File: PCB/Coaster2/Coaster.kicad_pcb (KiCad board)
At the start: 2 copper layers, 120 x 120 mm, 277 parts, among them J1 Reset, J2 TC2030-USB-NL-DS, J3 USB-C-Socket-H, U1 ICS43434_MEMS_Mic, U2 ESP32-S3-MINI-1, U3 MD8942

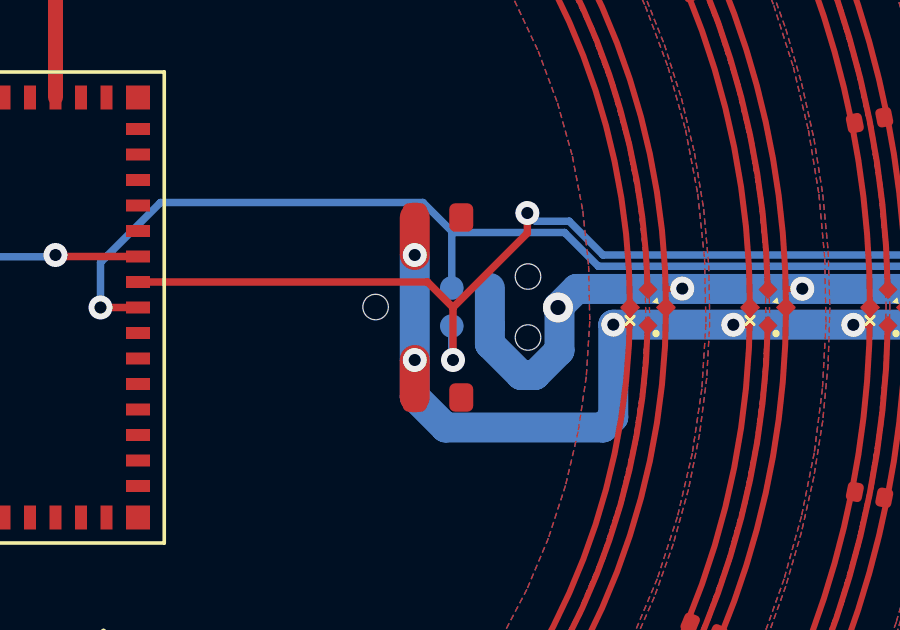
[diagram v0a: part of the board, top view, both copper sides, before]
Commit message: Fixed render
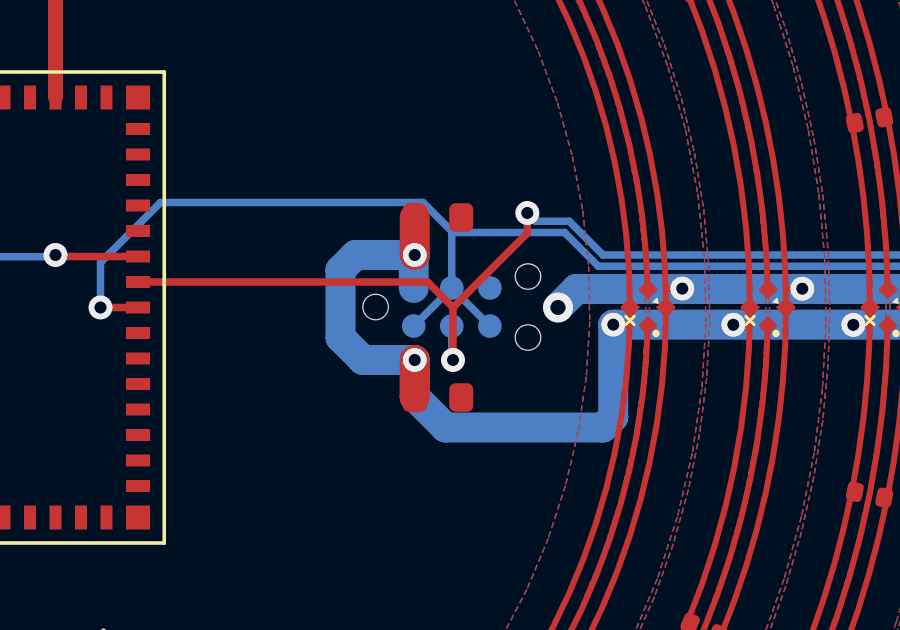
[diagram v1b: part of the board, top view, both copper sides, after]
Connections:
- J2 pad 2: VBUS -> D-
- J2 pad 6: GND -> D-
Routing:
- net GND: track 1099.9 -> 1093.5 mm
- net VBUS: track 1079.2 -> 1084.6 mm
- net D-: track 48.7 -> 52.3 mm
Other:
- board text added: "TC2030"

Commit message: Tidy
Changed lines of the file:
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@@
 	)
 	(gr_circle
+		(center 100 100)
+		(end 148 99.6)
+		(stroke
+			(width 1)
+			(type dot)
+		)
+		(fill no)
+		(layer "F.Mask")
+	)
+	(gr_circle
 		(center 80 134.641)
 		(end 85 134.641)
@@
 	)
 	(gr_circle
+		(center 100 100)
+		(end 78 100)
+		(stroke
+			(width 0.12)
+			(type dot)
+		)
+		(fill no)
+		(layer "B.SilkS")
+	)
+	(gr_circle
 		(center 140 100)
 		(end 140 95)
@@
 	)
 	(gr_circle
+		(center 100 100)
+		(end 51 100)
+		(stroke
+			(width 0.12)
+			(type dot)
+		)
+		(fill no)
+		(layer "B.SilkS")
+	)
+	(gr_circle
 		(center 140 100)
 		(end 143 100)
@@
 	)
 	(zone
-		(net 113)
-		(net_name "SD")
-		(layer "F.Cu")
-		(name "$teardrop_padvia$")
-		(hatch full 0.1)
-		(priority 30002)
-		(attr
-			(teardrop
-				(type padvia)
-			)
-		)
-		(connect_pads yes
-			(clearance 0)
-		)
-		(min_thickness 0.0254)
-		(filled_areas_thickness no)
-		(fill yes
-			(thermal_gap 0.5)
-			(thermal_bridge_width 0.5)
-			(island_removal_mode 1)
-			(island_area_min 10)
-		)
-		(polygon
-			(pts
-				(xy 100.334564 84.300341) (xy 100.511341 84.123564) (xy 100.3 83.71989) (xy 99.999293 83.788293)
-				(xy 99.89189 84.05)
-			)
-		)
-	)
-	(zone
 		(net 1)
 		(net_name "GND")
@@
 	)
 	(zone
-		(net 114)
-		(net_name "WS")
-		(layer "F.Cu")
-		(name "$teardrop_padvia$")
-		(hatch full 0.1)
-		(priority 30003)
-		(attr
-			(teardrop
-				(type padvia)
-			)
-		)
-		(connect_pads yes
-			(clearance 0)
-		)
-		(min_thickness 0.0254)
-		(filled_areas_thickness no)
-		(fill yes
-			(thermal_gap 0.5)
-			(thermal_bridge_width 0.5)
-			(island_removal_mode 1)
-			(island_area_min 10)
-		)
-		(polygon
-			(pts
-				(xy 100.775 84.311) (xy 101.025 84.311) (xy 101.161 84.012296) (xy 100.9 83.788) (xy 100.639 84.012296)
-			)
-		)
-	)
-	(zone
-		(net 2)
-		(net_name "+3V3")
-		(layer "F.Cu")
-		(name "$teardrop_padvia$")
-		(hatch full 0.1)
-		(priority 30000)
-		(attr
-			(teardrop
-				(type padvia)
-			)
-		)
-		(connect_pads yes
-			(clearance 0)
-		)
-		(min_thickness 0.0254)
-		(filled_areas_thickness no)
-		(fill yes
-			(thermal_gap 0.5)
-			(thermal_bridge_width 0.5)
-			(island_removal_mode 1)
-			(island_area_min 10)
-		)
-		(polygon
-			(pts
-				(xy 103.1625 111.6) (xy 103.103596 111.600725) (xy 102.907165 111.599072) (xy 102.798558 111.588917)
-				(xy 102.69297 111.567298) (xy 102.59786 111.53028) (xy 102.520689 111.473931) (xy 102.468915 111.394315)
-				(xy 102.454884 111.344553) (xy 102.45 111.2875) (xy 100.599 112) (xy 102.45 112.7125) (xy 102.454846 112.655657)
-				(xy 102.468771 112.60605) (xy 102.51997 112.526809) (xy 102.603622 112.466746) (xy 102.72734 112.423986)
-				(xy 102.9006 112.401291) (xy 103.103596 112.399275) (xy 103.1625 112.4)
-			)
-		)
-	)
-	(zone
 		(net 1)
 		(net_name "GND")
@@
 	)
 	(zone
+		(net 113)
+		(net_name "SD")
+		(layer "F.Cu")
+		(name "$teardrop_padvia$")
+		(hatch full 0.1)
+		(priority 30002)
+		(attr
+			(teardrop
+				(type padvia)
+			)
+		)
+		(connect_pads yes
+			(clearance 0)
+		)
+		(min_thickness 0.0254)
+		(filled_areas_thickness no)
+		(fill yes
+			(thermal_gap 0.5)
+			(thermal_bridge_width 0.5)
+			(island_removal_mode 1)
+			(island_area_min 10)
+		)
+		(polygon
+			(pts
+				(xy 100.334564 84.300341) (xy 100.511341 84.123564) (xy 100.3 83.71989) (xy 99.999293 83.788293)
+				(xy 99.89189 84.05)
+			)
+		)
+	)
+	(zone
+		(net 114)
+		(net_name "WS")
+		(layer "F.Cu")
+		(name "$teardrop_padvia$")
+		(hatch full 0.1)
+		(priority 30003)
+		(attr
+			(teardrop
+				(type padvia)
+			)
+		)
+		(connect_pads yes
+			(clearance 0)
+		)
+		(min_thickness 0.0254)
+		(filled_areas_thickness no)
+		(fill yes
+			(thermal_gap 0.5)
+			(thermal_bridge_width 0.5)
+			(island_removal_mode 1)
+			(island_area_min 10)
+		)
+		(polygon
+			(pts
+				(xy 100.775 84.311) (xy 101.025 84.311) (xy 101.161 84.012296) (xy 100.9 83.788) (xy 100.639 84.012296)
+			)
+		)
+	)
+	(zone
+		(net 2)
+		(net_name "+3V3")
+		(layer "F.Cu")
+		(name "$teardrop_padvia$")
+		(hatch full 0.1)
+		(priority 30000)
+		(attr
+			(teardrop
+				(type padvia)
+			)
+		)
+		(connect_pads yes
+			(clearance 0)
+		)
+		(min_thickness 0.0254)
+		(filled_areas_thickness no)
+		(fill yes
+			(thermal_gap 0.5)
+			(thermal_bridge_width 0.5)
+			(island_removal_mode 1)
+			(island_area_min 10)
+		)
+		(polygon
+			(pts
+				(xy 103.1625 111.6) (xy 103.103596 111.600725) (xy 102.907165 111.599072) (xy 102.798558 111.588917)
+				(xy 102.69297 111.567298) (xy 102.59786 111.53028) (xy 102.520689 111.473931) (xy 102.468915 111.394315)
+				(xy 102.454884 111.344553) (xy 102.45 111.2875) (xy 100.599 112) (xy 102.45 112.7125) (xy 102.454846 112.655657)
+				(xy 102.468771 112.60605) (xy 102.51997 112.526809) (xy 102.603622 112.466746) (xy 102.72734 112.423986)
+				(xy 102.9006 112.401291) (xy 103.103596 112.399275) (xy 103.1625 112.4)
+			)
+		)
+	)
+	(zone
+		(net 1)
+		(net_name "GND")
+		(layers "F&B.Cu")
+		(hatch edge 0.5)
+		(priority 1)
+		(connect_pads
+			(clearance 0.127)
+		)
+		(min_thickness 0.25)
+		(filled_areas_thickness no)
+		(fill yes
+			(thermal_gap 0.5)
+			(thermal_bridge_width 0.5)
+		)
+		(polygon
+			(pts
+				(xy 50 50) (xy 150 50) (xy 150 150) (xy 50 150)
+			)
+		)
+	)
+	(zone
 		(net 0)
 		(net_name "")
@@
 		(name "$teardrop_padvia$")
 		(hatch full 0.1)
-		(priority 30001)
-		(attr
-			(teardrop
-				(type padvia)
-			)
-		)
-		(connect_pads yes
-			(clearance 0)
-		)
-		(min_thickness 0.0254)
-		(filled_areas_thickness no)
-		(fill yes
-			(thermal_gap 0.5)
-			(thermal_bridge_width 0.5)
-			(island_removal_mode 1)
-			(island_area_min 10)
-		)
-		(polygon
-			(pts
-				(xy 118.266962 99.979185) (xy 118.090185 100.155962) (xy 118.40265 100.837728) (xy 118.730707 100.619707)
-				(xy 118.948728 100.29165)
-			)
-		)
-	)
-	(zone
-		(net 110)
-		(net_name "D-")
-		(layer "B.Cu")
-		(name "$teardrop_padvia$")
-		(hatch full 0.1)
 		(priority 30003)
 		(attr
@@
 		(name "$teardrop_padvia$")
 		(hatch full 0.1)
-		(priority 30005)
+		(priority 30001)
 		(attr
 			(teardrop
@@
 		(polygon
 			(pts
-				(xy 117.585 98.569165) (xy 117.335 98.569165) (xy 117.073865 99.272193) (xy 117.46 99.35) (xy 117.846135 99.272193)
+				(xy 118.266962 99.979185) (xy 118.090185 100.155962) (xy 118.40265 100.837728) (xy 118.730707 100.619707)
+				(xy 118.948728 100.29165)
+			)
+		)
+	)
+	(zone
+		(net 106)
+		(net_name "D+")
+		(layer "B.Cu")
+		(name "$teardrop_padvia$")
+		(hatch full 0.1)
+		(priority 30004)
+		(attr
+			(teardrop
+				(type padvia)
+			)
+		)
+		(connect_pads yes
+			(clearance 0)
+		)
+		(min_thickness 0.0254)
+		(filled_areas_thickness no)
+		(fill yes
+			(thermal_gap 0.5)
+			(thermal_bridge_width 0.5)
+			(island_removal_mode 1)
+			(island_area_min 10)
+		)
+		(polygon
+			(pts
+				(xy 117.335 101.398835) (xy 117.585 101.398835) (xy 117.846135 100.695807) (xy 117.46 100.618) (xy 117.073865 100.695807)
 			)
 		)
@@
 	)
 	(zone
-		(net 1)
-		(net_name "GND")
+		(net 110)
+		(net_name "D-")
 		(layer "B.Cu")
-		(hatch edge 0.5)
-		(priority 1)
-		(connect_pads
-			(clearance 0.127)
+		(name "$teardrop_padvia$")
+		(hatch full 0.1)
+		(priority 30005)
+		(attr
+			(teardrop
+				(type padvia)
+			)
 		)
-		(min_thickness 0.25)
+		(connect_pads yes
+			(clearance 0)
+		)
+		(min_thickness 0.0254)
 		(filled_areas_thickness no)
 		(fill yes
 			(thermal_gap 0.5)
 			(thermal_bridge_width 0.5)
+			(island_removal_mode 1)
+			(island_area_min 10)
 		)
 		(polygon
 			(pts
-				(xy 50 50) (xy 150 50) (xy 150 150) (xy 50 150)
+				(xy 117.585 98.569165) (xy 117.335 98.569165) (xy 117.073865 99.272193) (xy 117.46 99.35) (xy 117.846135 99.272193)
 			)
 		)
@@
 		(name "$teardrop_padvia$")
 		(hatch full 0.1)
-		(priority 30002)
+		(priority 30000)
 		(attr
 			(teardrop
@@
 		(polygon
 			(pts
-				(xy 116.829815 100.155962) (xy 116.653038 99.979185) (xy 115.971272 100.29165) (xy 116.189293 100.619707)
-				(xy 116.51735 100.837728)
+				(xy 117.923038 99.988815) (xy 118.099815 99.812038) (xy 117.78735 99.130272) (xy 117.459293 99.348293)
+				(xy 117.241272 99.67635)
 			)
 		)
 	)
 	(zone
-		(net 106)
-		(net_name "D+")
+		(net 110)
+		(net_name "D-")
 		(layer "B.Cu")
 		(name "$teardrop_padvia$")
 		(hatch full 0.1)
-		(priority 30004)
+		(priority 30002)
 		(attr
 			(teardrop
@@
 		(polygon
 			(pts
-				(xy 117.335 101.398835) (xy 117.585 101.398835) (xy 117.846135 100.695807) (xy 117.46 100.618) (xy 117.073865 100.695807)
+				(xy 116.829815 100.155962) (xy 116.653038 99.979185) (xy 115.971272 100.29165) (xy 116.189293 100.619707)
+				(xy 116.51735 100.837728)
 			)
 		)
@@
 			)
 		)
-	)
-	(zone
-		(net 110)
-		(net_name "D-")
-		(layer "B.Cu")
-		(name "$teardrop_padvia$")
-		(hatch full 0.1)
-		(priority 30000)
-		(attr
-			(teardrop
-				(type padvia)
-			)
-		)
-		(connect_pads yes
-			(clearance 0)
-		)
-		(min_thickness 0.0254)
-		(filled_areas_thickness no)
-		(fill yes
-			(thermal_gap 0.5)
-			(thermal_bridge_width 0.5)
-			(island_removal_mode 1)
-			(island_area_min 10)
-		)
-		(polygon
-			(pts
-				(xy 117.923038 99.988815) (xy 118.099815 99.812038) (xy 117.78735 99.130272) (xy 117.459293 99.348293)
-				(xy 117.241272 99.67635)
-			)
-		)

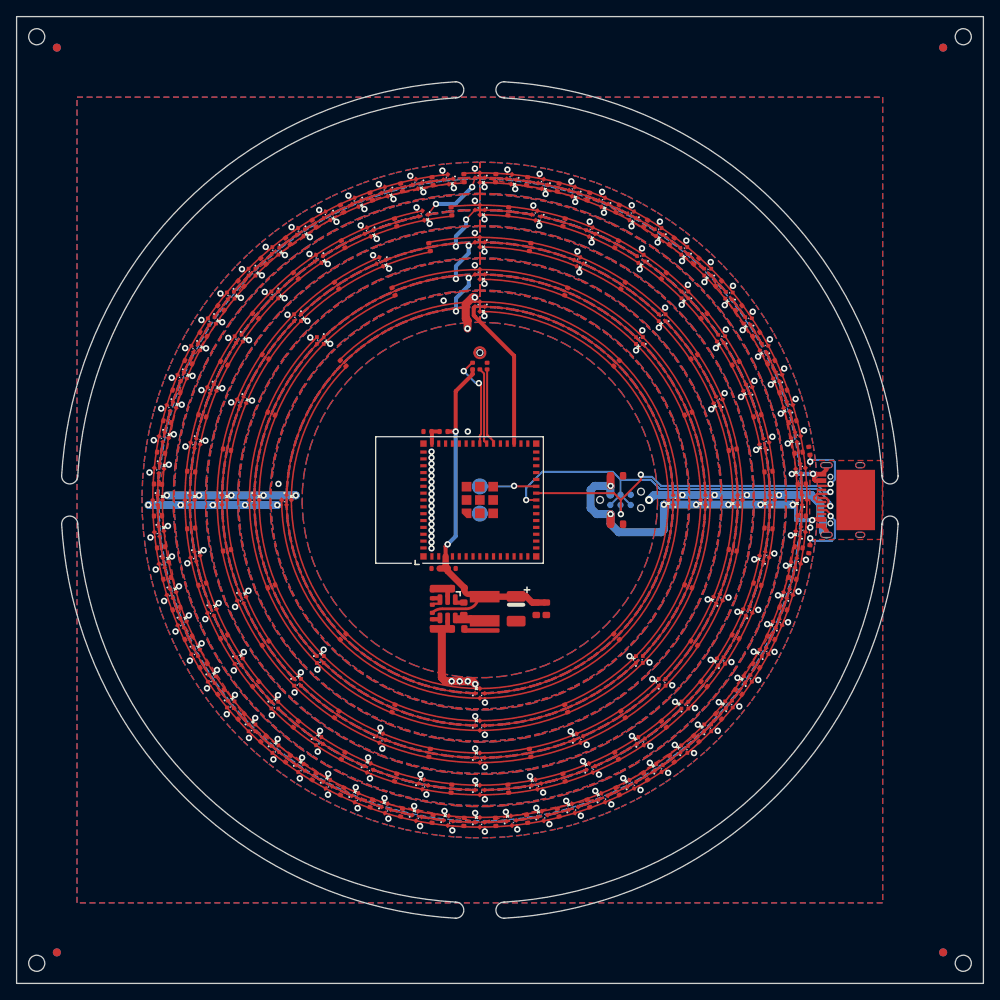
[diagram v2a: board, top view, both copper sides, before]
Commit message: WAGO power pads
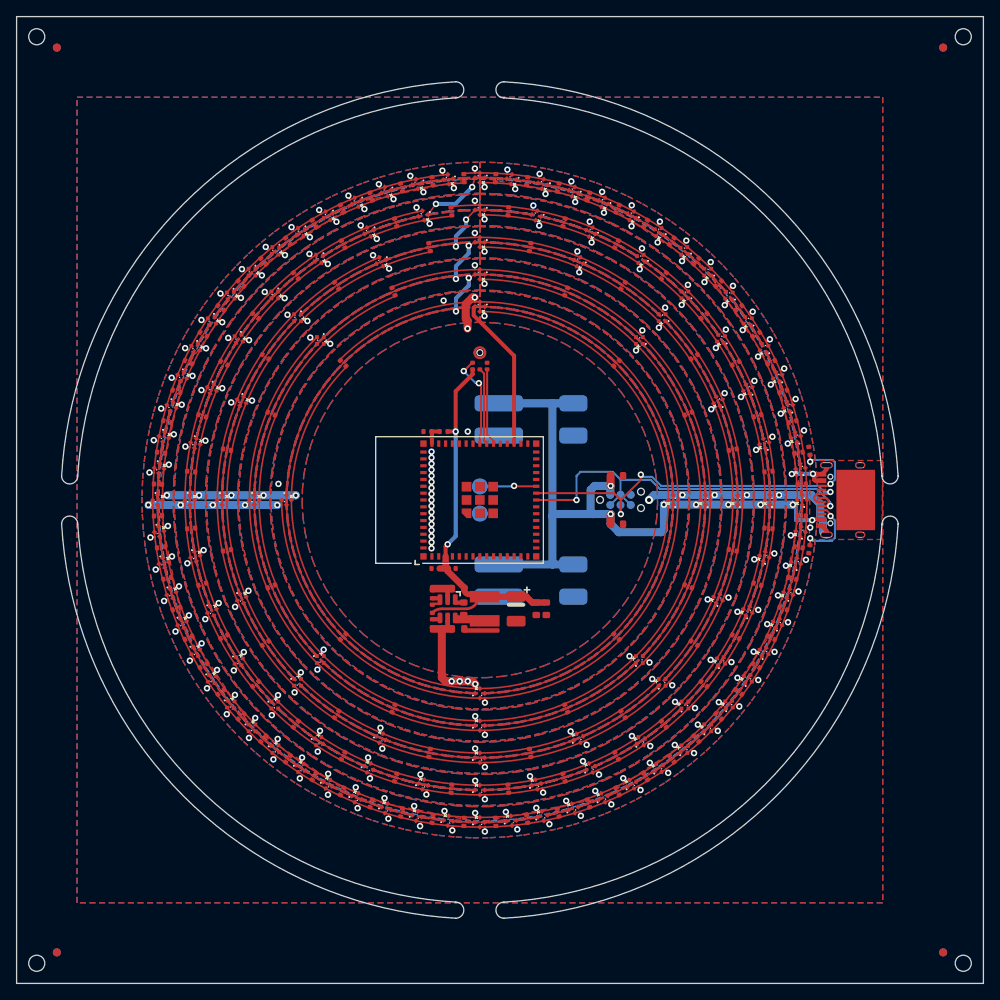
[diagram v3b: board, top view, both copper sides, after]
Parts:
- added J4: DC, RevK:WAGO-2060-452-998-404, B.Cu at (107.0, 110.0)
- added J5: DC, RevK:WAGO-2060-452-998-404, B.Cu at (107.0, 90.0)
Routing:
- net VBUS: track 1084.6 -> 1128.5 mm
- net D-: track 52.3 -> 50.6 mm
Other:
- board text added: "5V"
- board text added: "5V USB"
- board text added: "⏚"
- board text removed: "5V 2A"
